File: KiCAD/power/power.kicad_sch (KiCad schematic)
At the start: 0 parts

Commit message: KiCad revC: ±12V subsystem validated — LT1054 Fig-15 inverter + LM2940 LDO
Converged after iterating in LTspice:

* New standalone power project (KiCAD/power/) proves the topology before
  surgery on the analog project's power sheet. LT1054 as regulated inverter
  (not Figure 22 doubler — doubler was abandoned when single-FB-loop couldn't
  regulate both rails symmetrically). LM2940CT-12 LDO handles +12V from the
  13.8V bus. Both rails measure ±11.93V in sim at 1K load, VREF holds flat
  at 2.5V, V(FB_SD) settles at 0.596V.

* Datasheet-compliant divider values after discovering R16=10K violated the
  VREF ±100µA current limit: R16=20K, R17=240K (empirically tuned, differs
  from both my circuit analysis and datasheet formula — LTspice LT1054 model
  uses ~0.6V internal reference instead of the datasheet's 1.21V).
  C18=2.2nF loop comp matches datasheet "2 nF for all output voltages".

* New LM2940CT-12 symbol in xmitter.kicad_sym (TO-220-3, drop-in replacement
  for LM7812 pinout, 0.5V dropout vs 7812's 2V — needed for 13.8V-to-12V
  with headroom to spare).

* LTspice validation files in Documentation/:
    - power_sim.cir  (hand-written netlist, works in LTspice via File→Open)
    - power_sim.asc  (initial schematic attempt, retained as reference —
                      geometry is messy, use .cir instead)
    - Draft3.asc     (scratch for inspecting LT1054 symbol pin order)

Next step: migrate the validated topology into KiCAD/analog/power.kicad_sch,
replacing the shelved tube-era regulators (U15 LM317L, U19 LM7812, U23
LT1054) and the removed bridge rectifier that fed them.

Co-Authored-By: Claude Opus 4.7 <noreply@anthropic.com>
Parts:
- added C108: 220nF, Capacitor_THT:C_Disc_D6.0mm_W2.5mm_P5.00mm, symbol Device:C_US
- added C109: 0.47uF, Capacitor_THT:C_Rect_L7.0mm_W3.5mm_P5.00mm, symbol Device:C
- added C110: 0.1uF, Capacitor_THT:C_Disc_D5.0mm_W2.5mm_P5.00mm, symbol Device:C
- added C111: 22uF, Capacitor_THT:CP_Radial_D5.0mm_P2.00mm, symbol Device:C_Polarized
- added C17: 10uF, symbol Device:C_US
- added C18: 0.0022uF, symbol Device:C
- added C19: 100uF, symbol Device:C_Polarized_US
- added C20: 10uF, symbol Device:C_Polarized_US
- added J4: Screw_Terminal_01x02, symbol Connector:Screw_Terminal_01x02
- added R16: 20K, symbol Device:R_US
- added R17: 240K, symbol Device:R_US
- added U7: LT1054, symbol Regulator_SwitchedCapacitor:LT1054
- added U8: LM2940CT-12, Package_TO_SOT_THT:TO-220-3_Vertical, symbol xmitter:LM2940CT-12
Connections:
- new net: C108.1, C109.1, C17.1, J4.2 (Pin_2), U7.8 (V+), U8.1 (VI)
- new net: C18.2, R16.1, R17.1, U7.1 (FB/SHDN)
- new net: C20.1, U7.2 (CAP+)
- new net: C20.2, U7.4 (CAP-)
- new net: R16.2, U7.6 (VREF)
- new net +12V: C110.1, C111.1, U8.3 (VO)
- new net -12V: C18.1, C19.2, R17.2, U7.5 (-VOUT)
- new net GND: C108.2, C109.2, C110.2, C111.2, C17.2, C19.1, J4.1 (Pin_1), U7.3 (GND), U8.2 (GND)
- no-connect marks 0 -> 1
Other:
- note added: "13.8V in"
- note added: "R17=R16(Vout/1.21V+1)"

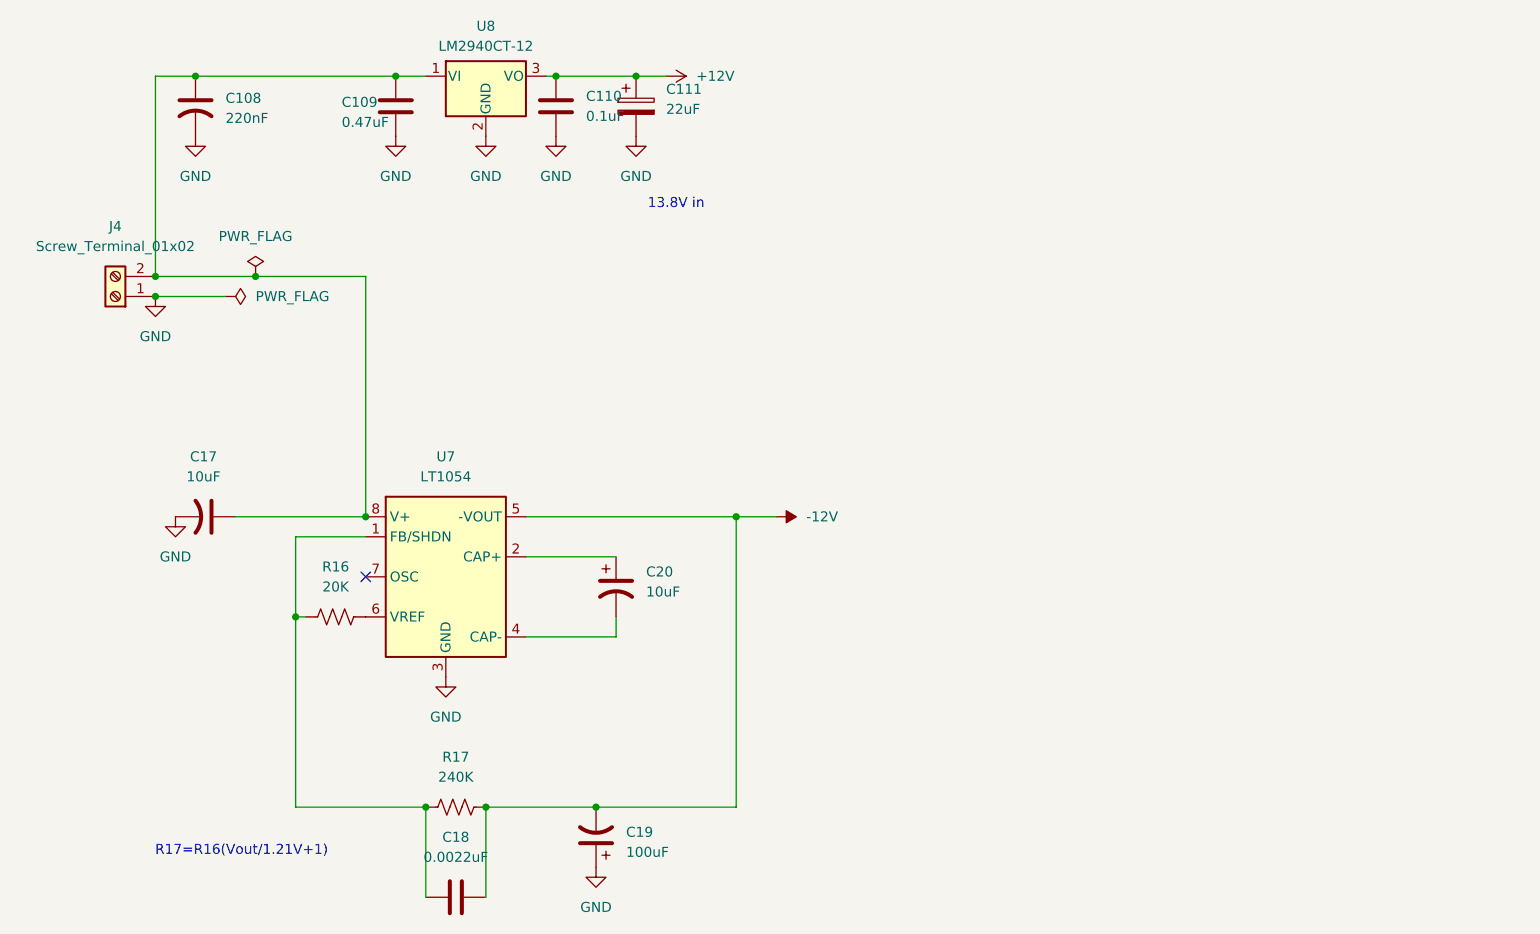
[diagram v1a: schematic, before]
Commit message: KiCad revC: +28V doubler + 5V LDO added to analog/power, ERC clean
- Migrated LT1054 Figure 20 positive doubler from standalone power project
  into analog/power.kicad_sch for the +28V reed-relay rail
- Added LM2940CT-5.0 LDO stage for Metro / Si5351 +5V rail
- analog ERC: 4 messages, all classified as false positives (U9 pin 5
  tied to GND per Fig 20 topology, PCF_P5_SPARE intentionally unused,
  VIN pins now driven by added +5V rail)
- Added QRP Labs 10W PA / 5W PA reference PDFs + 2N7000 + lm2940c
  datasheets to Documentation/QRP_Examples/

Co-Authored-By: Claude Opus 4.7 <noreply@anthropic.com>
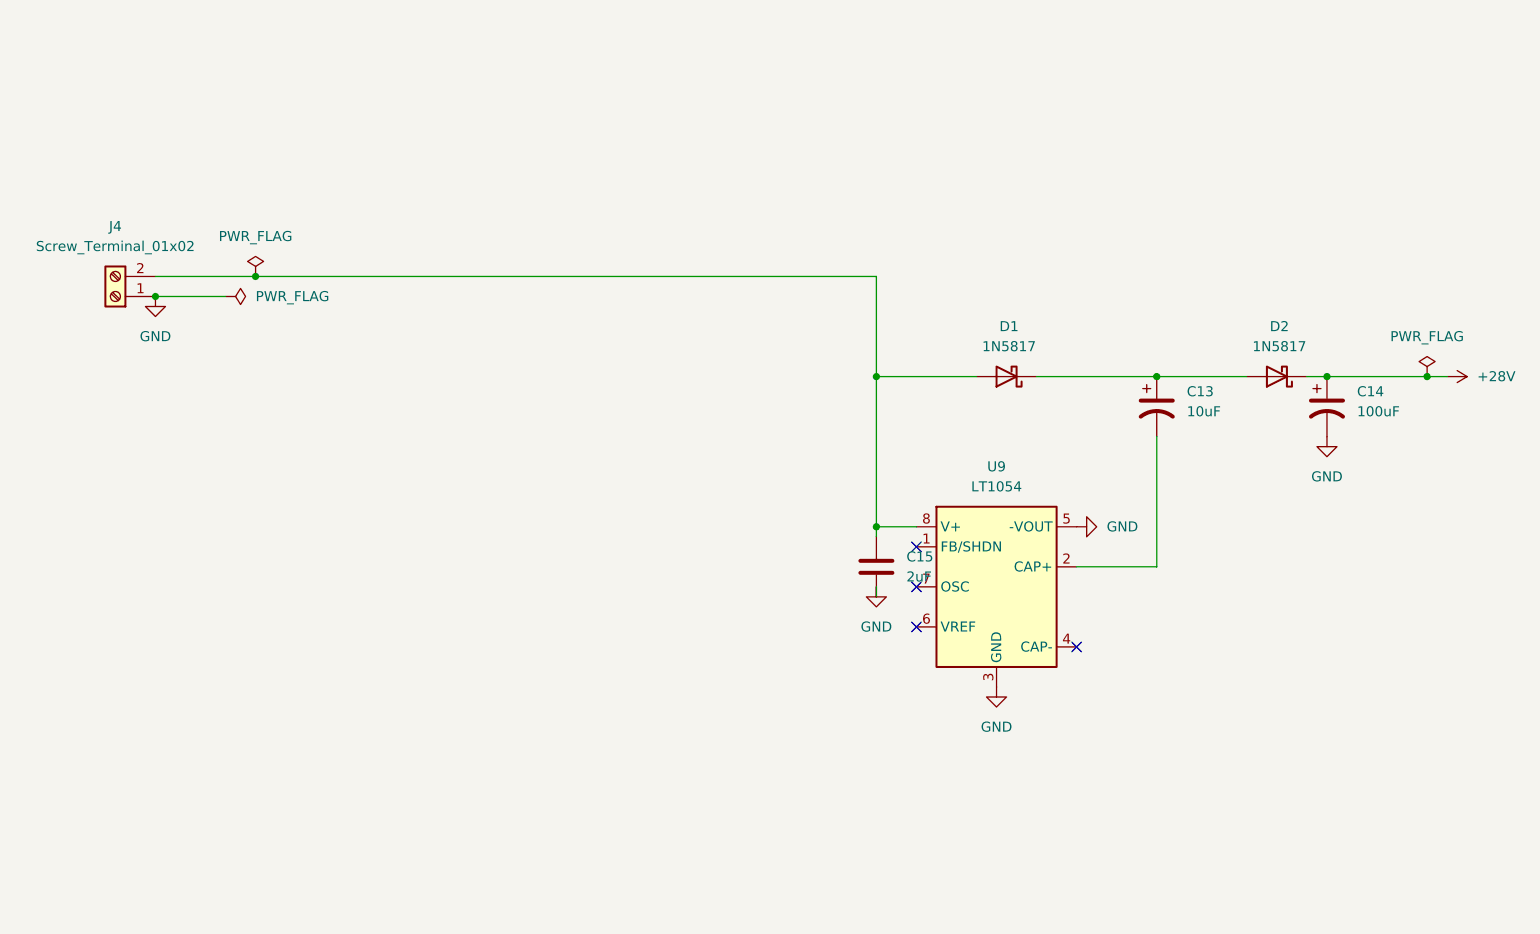
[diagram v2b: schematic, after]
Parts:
- removed C108: 220nF, Capacitor_THT:C_Disc_D6.0mm_W2.5mm_P5.00mm, symbol Device:C_US
- removed C109: 0.47uF, Capacitor_THT:C_Rect_L7.0mm_W3.5mm_P5.00mm, symbol Device:C
- removed C110: 0.1uF, Capacitor_THT:C_Disc_D5.0mm_W2.5mm_P5.00mm, symbol Device:C
- removed C111: 22uF, Capacitor_THT:CP_Radial_D5.0mm_P2.00mm, symbol Device:C_Polarized
- removed C17: 10uF, symbol Device:C_US
- removed C18: 0.0022uF, symbol Device:C
- removed C19: 100uF, symbol Device:C_Polarized_US
- removed C20: 10uF, symbol Device:C_Polarized_US
- removed R16: 20K, symbol Device:R_US
- removed R17: 240K, symbol Device:R_US
- removed U7: LT1054, symbol Regulator_SwitchedCapacitor:LT1054
- removed U8: LM2940CT-12, Package_TO_SOT_THT:TO-220-3_Vertical, symbol xmitter:LM2940CT-12
- added C13: 10uF, symbol Device:C_Polarized_US
- added C14: 100uF, symbol Device:C_Polarized_US
- added C15: 2uF, symbol Device:C
- added D1, D2: 1N5817, Diode_THT:D_DO-41_SOD81_P10.16mm_Horizontal, symbol Diode:1N5817
- added U9: LT1054, symbol Regulator_SwitchedCapacitor:LT1054
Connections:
- net GND: now also C14.2, C15.2, U9.3 (GND), U9.5 (-VOUT)
- net at J4.2 (Pin_2): now also C15.1, D1.2 (A), U9.8 (V+)
- new net: C13.1, D1.1 (K), D2.2 (A)
- new net: C13.2, U9.2 (CAP+)
- new net +28V: C14.1, D2.1 (K)
- no-connect marks 1 -> 4
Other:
- note removed: "13.8V in"
- note removed: "R17=R16(Vout/1.21V+1)"

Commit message: revD: footprint pass across all boards + ss_pa fault-chain fix + LLM review brief
- New tools/assign_misc_footprints.py: lib_id-keyed footprint assigner
  (resistors, screw terminals, pin headers, LT1054); mirrors cap-script
  safe-write (UTF-8 no BOM, no CRLF translation).
- tools/assign_cap_footprints.py: added 0.47uF -> C_Rect_L7.0mm case.
- Ran both scripts across analog, ss_pa, Output LPF, frontpanel,
  protoshield, and shelved power board. ~100 fills; details in diffs.
- ss_pa: R1-R4 (0.22 ohm source sense) upgraded to 2W Yageo RSF200
  with DIN0516 L15.5mm/P20.32mm footprint; Value tagged "0.22R 2W".
  R15/R16 confirmed 1/4W (DIN0207) for BS170 source degeneration.
- analog/power: R44 15R 5W horizontal, P30.48mm footprint.
- ss_pa fault chain (from external LLM review): R21/R22 raised
  10K -> 100K to restore self-latching loop gain; new R26 = 100K
  across C12 so cap discharges between power cycles (reliable reset).
  R26 footprint pending.
- Documentation/revD_llm_review_brief.md: new, comprehensive system
  description for external LLM deep-dive (function, component values,
  power dissipation, design flaws). References all five board netlists.

Co-Authored-By: Claude Opus 4.7 <noreply@anthropic.com>
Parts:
- C13: footprint (none) -> Capacitor_THT:CP_Radial_D5.0mm_P2.00mm
- C14: footprint (none) -> Capacitor_THT:CP_Radial_D8.0mm_P5.00mm
- C15: footprint (none) -> Capacitor_THT:C_Rect_L7.2mm_W4.5mm_P5.00mm
- J4: footprint (none) -> TerminalBlock_Phoenix:TerminalBlock_Phoenix_MKDS-1,5-2_1x02_P5.00mm_Horizontal
- U9: footprint (none) -> Package_DIP:DIP-8_W7.62mm
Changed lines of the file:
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@@
 			)
 		)
-		(property "Footprint" ""
+		(property "Footprint" "Capacitor_THT:CP_Radial_D8.0mm_P5.00mm"
 			(at 255.27 82.55 0)
 			(hide yes)
@@
 			)
 		)
-		(property "Footprint" ""
+		(property "Footprint" "Package_DIP:DIP-8_W7.62mm"
 			(at 215.9 107.95 0)
 			(hide yes)
@@
 			)
 		)
-		(property "Footprint" ""
+		(property "Footprint" "Capacitor_THT:C_Rect_L7.2mm_W4.5mm_P5.00mm"
 			(at 199.0852 106.68 0)
 			(hide yes)
@@
 			)
 		)
-		(property "Footprint" ""
+		(property "Footprint" "TerminalBlock_Phoenix:TerminalBlock_Phoenix_MKDS-1,5-2_1x02_P5.00mm_Horizontal"
 			(at 101.6 68.58 0)
 			(hide yes)
@@
 			)
 		)
-		(property "Footprint" ""
+		(property "Footprint" "Capacitor_THT:CP_Radial_D5.0mm_P2.00mm"
 			(at 233.68 82.55 0)
 			(hide yes)
